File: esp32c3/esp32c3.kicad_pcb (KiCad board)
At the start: 2 copper layers, 20.9 x 32.9 mm, 29 parts, among them J1 A1501WR-S-2P, J2 Conn_01x06, J3 Conn_01x05, SW1 wake up, U1 ESP32-C3-WROOM-02, U2 AHT10, U3 LIS2DH, U4 HX6306

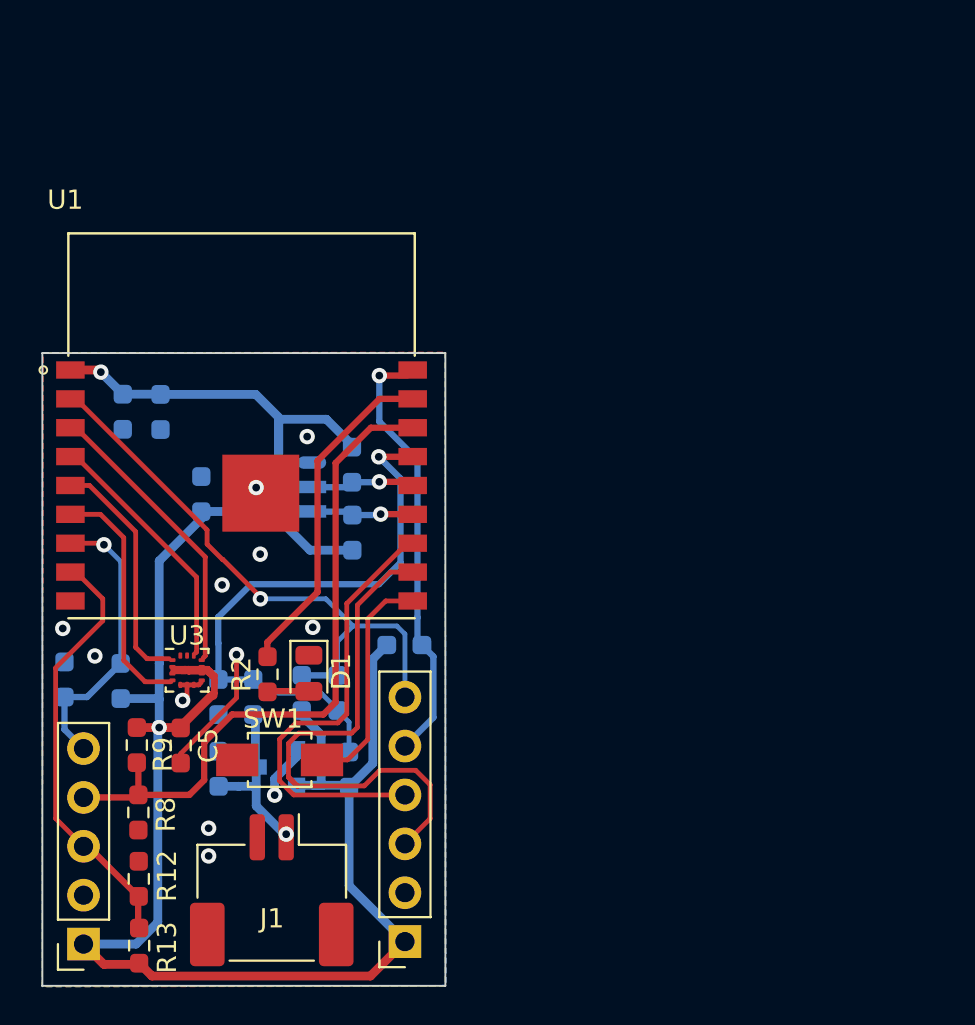
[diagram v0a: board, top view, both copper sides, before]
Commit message: Place components on one side
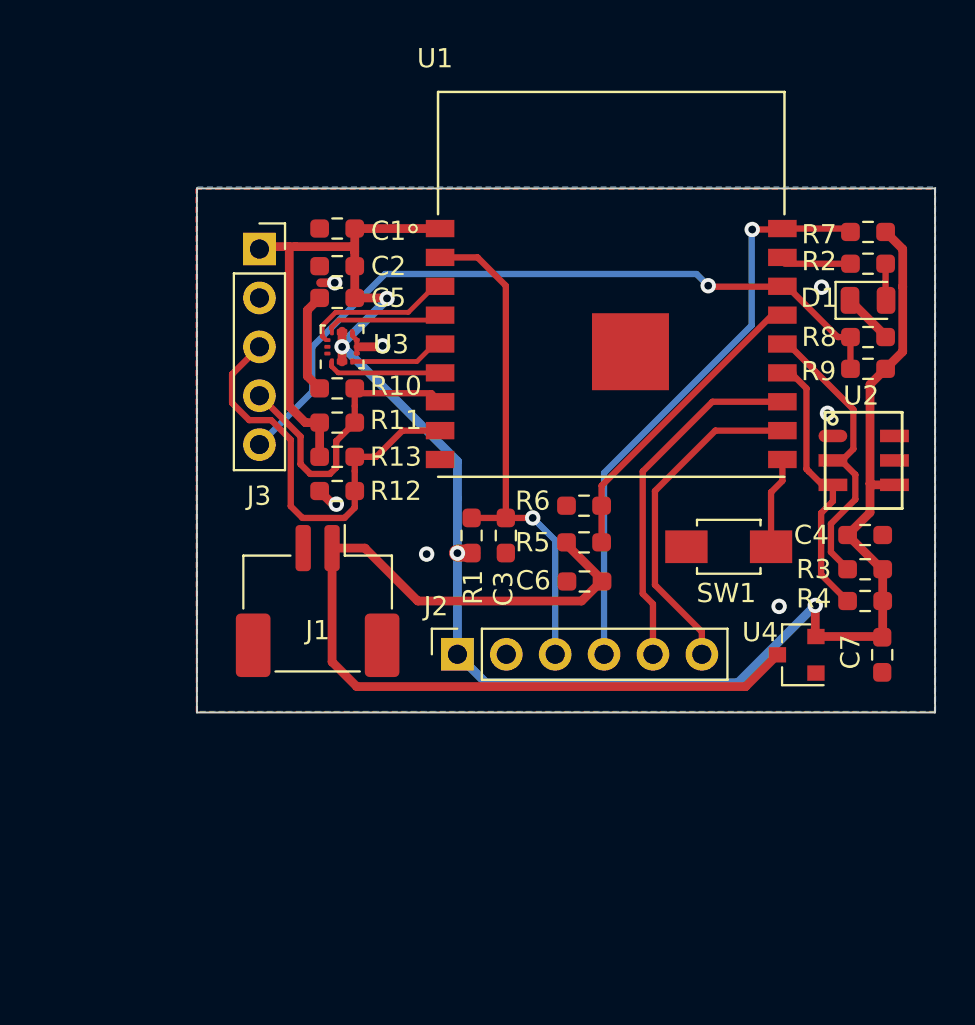
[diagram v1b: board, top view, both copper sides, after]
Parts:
- C1, C2, C3, C4, C6, C7, R1, R10, R11, R3, R4, R5, R6, R7, U2, U4: moved to F.Cu
- moved R8 45.2 mm to (75.8, 76.7), turned to 0 degrees
- moved R9 42.7 mm to (75.8, 78.4), turned to 0 degrees
- moved R2 37.8 mm to (75.8, 72.9), turned to 0 degrees
- moved J3 37.3 mm to (44.2, 72.1), turned to 0 degrees
- moved D1 34.9 mm to (75.8, 74.8), turned to 0 degrees
- moved C4 34.6 mm to (75.7, 87.0), turned to 0 degrees
- moved R7 32.3 mm to (75.8, 71.2), turned to 0 degrees
- moved U2 31.0 mm to (75.9, 83.1), turned to 0 degrees
- moved C7 28.3 mm to (76.6, 93.2), turned to -90 degrees
- moved U4 27.6 mm to (72.1, 93.2)
- moved R13 27.4 mm to (48.3, 82.9), turned to 180 degrees
- moved R3 27.2 mm to (75.7, 88.8), turned to 180 degrees
- moved R4 26.9 mm to (75.7, 90.4), turned to 180 degrees
- moved SW1 25.8 mm to (68.6, 87.6)
- moved C5 24.6 mm to (48.3, 74.7), turned to 180 degrees
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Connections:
- J2 pad 3: RXD -> EN
- J2 pad 4: TXD -> IO0
- J2 pad 5: IO0 -> TXD
- J2 pad 6: EN -> RXD
- J3 pad 4: IO2 -> IO8
- J3 pad 5: IO8 -> IO2
- U1 pad 3: INT2 -> INT1
- U1 pad 4: INT1 -> INT2
- U1 pad 5: SCL -> SDA
- U1 pad 6: SDA -> SCL
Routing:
- net V_In: track 8.96 -> 48.7 mm, vias 1 -> 0
- net LED: track 17.7 -> 3.88 mm
- net 3.3V: track 116.4 -> 102.8 mm, vias 2 -> 4
- net RXD: track 28.8 -> 17.4 mm
- net SDA_AHT10: track 5.29 -> 15.9 mm, vias 1 -> 0
- net SCL_AHT10: track 5.19 -> 14.4 mm, vias 1 -> 0
- net INT2: track 15.1 -> 5.98 mm
- net INT: track 12.7 -> 4.78 mm
- net IO0: track 23.2 -> 31.0 mm
- net SDA: track 12.6 -> 4.92 mm
- net ADC: track 23.4 -> 16.0 mm, vias 1 -> 0
- net SCL: track 12.4 -> 6.03 mm
- net GND: track 17.7 -> 12.3 mm, vias 12 -> 7
- net INT1: track 13.1 -> 7.74 mm
- net TXD: track 23.5 -> 18.5 mm
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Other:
- board size 20.9 x 32.9 mm -> 38.4 x 27.2 mm

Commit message: Complete LIS2DH12 modification
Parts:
- added C8: 0.1uF, Resistor_SMD:R_0603_1608Metric_Pad0.98x0.95mm_HandSolder, F.Cu at (47.9, 75.0)
- added C9: 0.1uF, Resistor_SMD:R_0603_1608Metric_Pad0.98x0.95mm_HandSolder, F.Cu at (47.9, 77.6)
- C5: value 100nF -> 10uF
- U3: footprint Package_LGA:LGA-14_2x2mm_P0.35mm_LayoutBorder3x4y -> Package_LGA:LGA-12_2x2mm_P0.5mm
- moved C2 2.80 mm to (50.9, 72.0), turned to 90 degrees
- moved U3 2.62 mm to (51.1, 77.2)
- moved C5 1.69 mm to (47.9, 73.0)
- moved C1 0.38 mm to (47.9, 71.1)
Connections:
- U3 pad 3: 3.3V -> GND
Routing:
- net GND: track 12.3 -> 3.82 mm, vias 7 -> 5
- net 3.3V: track 102.8 -> 97.7 mm
- net SDA: track 4.92 -> 2.55 mm
- net SCL: track 6.03 -> 3.81 mm
- net INT2: track 5.98 -> 5.17 mm
- net INT1: track 7.74 -> 7.05 mm
- removed copper zone on B.Cu, net GND
- removed copper zone on F.Cu, net GND

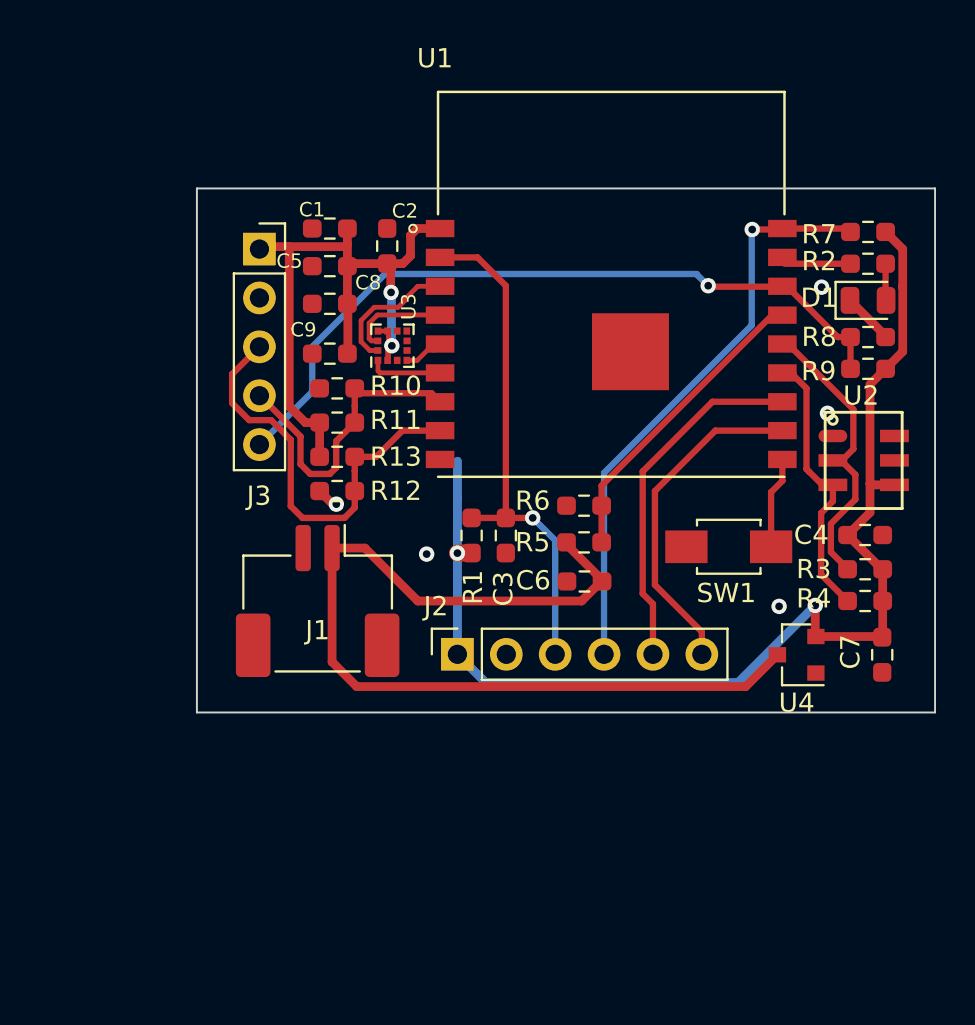
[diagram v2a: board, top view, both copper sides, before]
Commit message: Complete LIS2DH12 modification
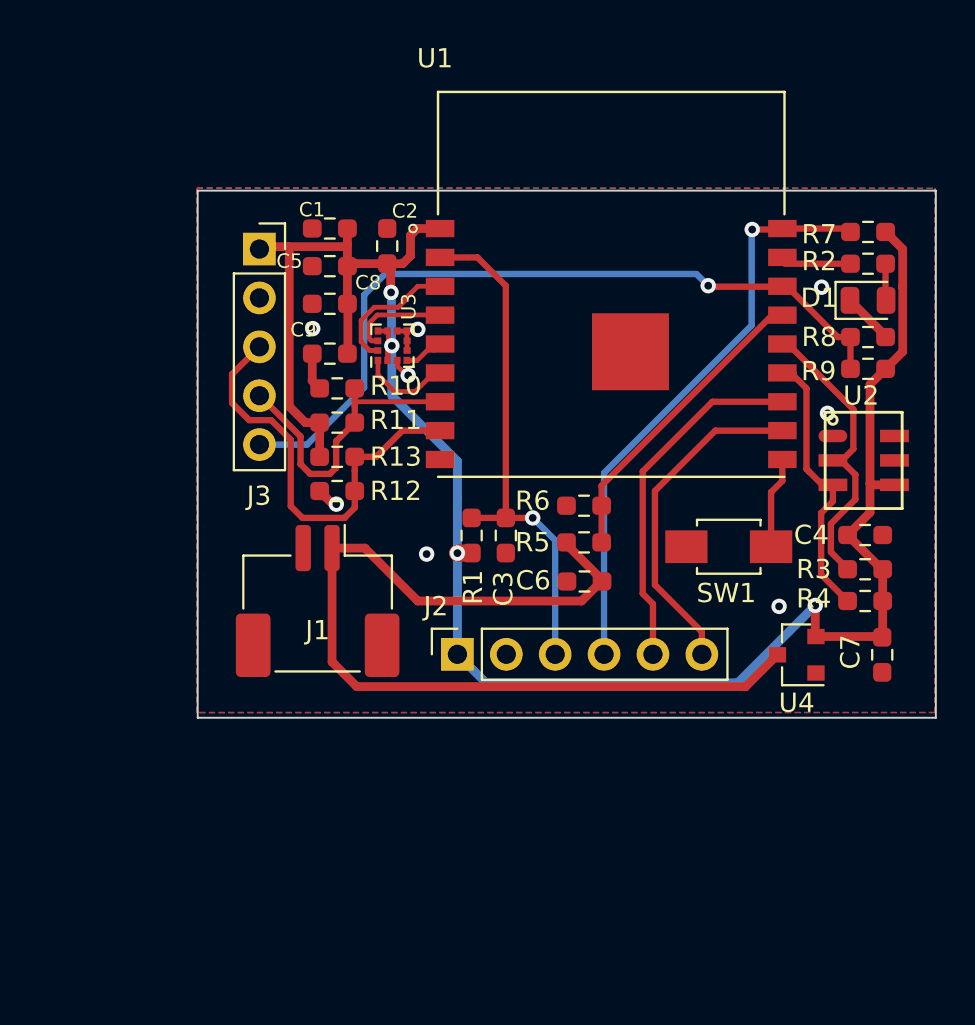
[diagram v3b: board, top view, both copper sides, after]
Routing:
- net 3.3V: track 97.7 -> 105.1 mm
- net GND: track 3.82 -> 8.98 mm, vias 5 -> 8
- net IO2: track 38.8 -> 40.2 mm
- net SCL: track 3.81 -> 5.19 mm
- added copper zone on B.Cu, net GND
- added copper zone on F.Cu, net GND
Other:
- board size 38.4 x 27.2 mm -> 38.4 x 27.4 mm
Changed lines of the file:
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@@
     )
   )
-  (gr_rect (start 40.9702 68.9864) (end 79.3242 96.2152) (layer "Edge.Cuts") (width 0.1) (fill none))
+  (gr_rect (start 41.013 69.1012) (end 79.367 96.49) (layer "Edge.Cuts") (width 0.1) (fill none))
   (segment (start 76.604495 88.773) (end 76.604495 90.424) (width 0.4572) (layer "F.Cu") (net 1))
   (segment (start 74.779505 86.82449) (end 74.77951 86.82449) (width 0.4572) (layer "F.Cu") (net 1))
@@
   (segment (start 54.507994 83.160006) (end 54.507994 85.090406) (width 0.4572) (layer "B.Cu") (net 1))
   (segment (start 51.06 74.39) (end 51.08 74.41) (width 0.4572) (layer "B.Cu") (net 1))
+  (segment (start 51.100126 77.161161) (end 51.100126 79.752139) (width 0.4572) (layer "B.Cu") (net 1))
   (segment (start 51.08 74.41) (end 51.08 77.141024) (width 0.4572) (layer "B.Cu") (net 1))
   (segment (start 54.507994 87.935206) (end 54.507994 93.193006) (width 0.4572) (layer "B.Cu") (net 1))
   (segment (start 69.088 94.6658) (end 55.9808 94.6658) (width 0.4572) (layer "B.Cu") (net 1))
+  (segment (start 51.100126 79.752139) (end 54.507994 83.160006) (width 0.4572) (layer "B.Cu") (net 1))
   (segment (start 48.029673 85.391193) (end 47.347505 84.709) (width 0.4572) (layer "F.Cu") (net 2))
+  (segment (start 52.365504 76.394496) (end 52.45 76.31) (width 0.25) (layer "F.Cu") (net 2))
   (segment (start 76.75499 76.653009) (end 74.904981 74.803) (width 0.4572) (layer "F.Cu") (net 2))
+  (segment (start 51.879997 76.394496) (end 52.365504 76.394496) (width 0.25) (layer "F.Cu") (net 2))
+  (segment (start 51.379997 76.394496) (end 51.879997 76.394496) (width 0.25) (layer "F.Cu") (net 2))
+  (segment (start 47.347505 79.375) (end 46.949995 78.97749) (width 0.4572) (layer "F.Cu") (net 2))
+  (segment (start 51.95 78.7) (end 51.87 78.7) (width 0.25) (layer "F.Cu") (net 2))
+  (segment (start 51.879997 76.894496) (end 51.892497 76.906996) (width 0.25) (layer "F.Cu") (net 2))
   (segment (start 48.215383 85.391184) (end 48.029684 85.391184) (width 0.25) (layer "F.Cu") (net 2))
   (segment (start 76.754995 76.708) (end 76.754995 76.653005) (width 0.25) (layer "F.Cu") (net 2))
+  (segment (start 46.95 78.9775) (end 46.9665 78.961) (width 0.25) (layer "F.Cu") (net 2))
+  (segment (start 46.966505 78.961005) (end 46.966505 77.5716) (width 0.4572) (layer "F.Cu") (net 2))
+  (segment (start 51.87 78.7) (end 51.379997 78.209997) (width 0.25) (layer "F.Cu") (net 2))
+  (segment (start 51.892497 76.906996) (end 51.892497 77.406996) (width 0.25) (layer "F.Cu") (net 2))
+  (segment (start 51.879997 76.394496) (end 51.879997 76.894496) (width 0.25) (layer "F.Cu") (net 2))
+  (segment (start 51.379997 78.209997) (end 51.379997 77.919496) (width 0.25) (layer "F.Cu") (net 2))
+  (via (at 51.95 78.7) (size 0.8) (drill 0.4) (layers "F.Cu" "B.Cu") (free) (net 2))
+  (via (at 52.45 76.31) (size 0.8) (drill 0.4) (layers "F.Cu" "B.Cu") (free) (net 2))
   (via (at 52.9082 87.9856) (size 0.8) (drill 0.4) (layers "F.Cu" "B.Cu") (free) (net 2))
   (via (at 71.2216 90.7034) (size 0.8) (drill 0.4) (layers "F.Cu" "B.Cu") (free) (net 2))
@@
   (via (at 73.4314 74.1172) (size 0.8) (drill 0.4) (layers "F.Cu" "B.Cu") (free) (net 2))
   (via (at 48.215383 85.391184) (size 0.8) (drill 0.4) (layers "F.Cu" "B.Cu") (free) (net 2))
+  (via (at 46.99 76.27) (size 0.8) (drill 0.4) (layers "F.Cu" "B.Cu") (free) (net 2))
   (segment (start 53.607487 72.57001) (end 55.55201 72.57001) (width 0.3302) (layer "F.Cu") (net 3))
   (segment (start 55.245 86.106) (end 57.023 86.106) (width 0.3302) (layer "F.Cu") (net 3))
@@
   (segment (start 71.631607 74.070007) (end 74.2696 76.708) (width 0.3302) (layer "F.Cu") (net 8))
   (via (at 67.5386 74.041) (size 0.8) (drill 0.4) (layers "F.Cu" "B.Cu") (net 8))
-  (segment (start 50.7492 73.4314) (end 46.9646 77.216) (width 0.3302) (layer "B.Cu") (net 8))
-  (segment (start 46.9646 77.216) (end 46.9646 79.552394) (width 0.3302) (layer "B.Cu") (net 8))
+  (segment (start 46.694 82.296) (end 44.220994 82.296) (width 0.3302) (layer "B.Cu") (net 8))
+  (segment (start 50.7492 73.4314) (end 49.66 74.5206) (width 0.3302) (layer "B.Cu") (net 8))
+  (segment (start 49.66 79.33) (end 46.694 82.296) (width 0.3302) (layer "B.Cu") (net 8))
+  (segment (start 66.929 73.4314) (end 50.7492 73.4314) (width 0.3302) (layer "B.Cu") (net 8))
   (segment (start 67.5386 74.041) (end 66.929 73.4314) (width 0.3302) (layer "B.Cu") (net 8))
-  (segment (start 46.9646 79.552394) (end 44.220994 82.296) (width 0.3302) (layer "B.Cu") (net 8))
-  (segment (start 66.929 73.4314) (end 50.7492 73.4314) (width 0.3302) (layer "B.Cu") (net 8))
+  (segment (start 49.66 74.5206) (end 49.66 79.33) (width 0.3302) (layer "B.Cu") (net 8))
   (segment (start 48.2092 83.4898) (end 48.2092 82.1163) (width 0.3302) (layer "F.Cu") (net 9))
   (segment (start 46.355 81.871268) (end 46.355 83.312) (width 0.3302) (layer "F.Cu") (net 9))
+  (segment (start 53.6075 80.07) (end 49.22 80.07) (width 0.25) (layer "F.Cu") (net 9))
   (segment (start 44.221 79.756) (end 44.239732 79.756) (width 0.3302) (layer "F.Cu") (net 9))
+  (segment (start 49.172495 79.375) (end 49.172495 80.022495) (width 0.3302) (layer "F.Cu") (net 9))
+  (segment (start 49.172495 80.022495) (end 49.172495 80.287495) (width 0.3302) (layer "F.Cu") (net 9))
   (segment (start 46.863 83.82) (end 47.879 83.82) (width 0.3302) (layer "F.Cu") (net 9))
   (segment (start 46.355 83.312) (end 46.863 83.82) (width 0.3302) (layer "F.Cu") (net 9))
   (segment (start 44.239732 79.756) (end 46.355 81.871268) (width 0.3302) (layer "F.Cu") (net 9))
   (segment (start 47.879 83.82) (end 48.2092 83.4898) (width 0.3302) (layer "F.Cu") (net 9))
-  (segment (start 49.172495 79.375) (end 49.172495 80.287495) (width 0.3302) (layer "F.Cu") (net 9))
-  (segment (start 49.4265 79.629) (end 53.166493 79.629) (width 0.3302) (layer "F.Cu") (net 9))
-  (segment (start 53.166493 79.629) (end 53.293493 79.756) (width 0.3302) (layer "F.Cu") (net 9))
   (segment (start 48.2092 82.1163) (end 49.1725 81.153) (width 0.3302) (layer "F.Cu") (net 9))
+  (segment (start 49.22 80.07) (end 49.172495 80.022495) (width 0.25) (layer "F.Cu") (net 9))
   (segment (start 49.172495 80.287495) (end 49.172495 81.153) (width 0.3302) (layer "F.Cu") (net 9))
-  (segment (start 49.1725 79.375) (end 49.4265 79.629) (width 0.3302) (layer "F.Cu") (net 9))
   (segment (start 53.2935 79.756) (end 53.6075 80.07) (width 0.25) (layer "F.Cu") (net 9))
   (segment (start 42.799 78.637994) (end 42.799 80.137) (width 0.3302) (layer "F.Cu") (net 10))
@@
   (segment (start 53.2775 77.4) (end 53.6075 77.07) (width 0.25) (layer "F.Cu") (net 16))
   (segment (start 53.268992 77.07) (end 52.419496 77.919496) (width 0.25) (layer "F.Cu") (net 16))
-  (segment (start 53.6075 78.57) (end 50.49 78.57) (width 0.25) (layer "F.Cu") (net 17))
-  (segment (start 50.379997 78.459997) (end 50.379997 77.919496) (width 0.25) (layer "F.Cu") (net 17))
-  (segment (start 50.49 78.57) (end 50.379997 78.459997) (width 0.25) (layer "F.Cu") (net 17))
+  (segment (start 53.28 78.57) (end 53.6075 78.57) (width 0.25) (layer "F.Cu") (net 17))
+  (segment (start 52.31 79.54) (end 53.28 78.57) (width 0.25) (layer "F.Cu") (net 17))
+  (segment (start 51.25 79.54) (end 52.31 79.54) (width 0.25) (layer "F.Cu") (net 17))
+  (segment (start 50.379997 77.919496) (end 50.379997 78.669997) (width 0.25) (layer "F.Cu") (net 17))
+  (segment (start 50.379997 78.669997) (end 51.25 79.54) (width 0.25) (layer "F.Cu") (net 17))
+  (segment (start 53.6075 78.57) (end 53.2875 78.89) (width 0.25) (layer "F.Cu") (net 17))
   (segment (start 49.5 75.844688) (end 49.5 76.95) (width 0.25) (layer "F.Cu") (net 18))
   (segment (start 50.184424 75.160264) (end 49.5 75.844688) (width 0.25) (layer "F.Cu") (net 18))
@@
   (segment (start 62.02299 89.32799) (end 62.02299 89.408) (width 0.4572) (layer "F.Cu") (net 21))
   (segment (start 52.451 90.424) (end 49.700993 87.673993) (width 0.4572) (layer "F.Cu") (net 21))
+  (zone (net 2) (net_name "GND") (layer "F.Cu") (hatch edge 0.508)
+    (connect_pads (clearance 0.508))
+    (min_thickness 0.254) (filled_areas_thickness no)
+    (fill yes (thermal_gap 0.508) (thermal_bridge_width 0.508))
+    (polygon
+      (pts
+        (xy 79.32 68.98)
+        (xy 79.31 96.21)
+        (xy 40.97 96.21)
+        (xy 40.97 68.96)
+      )
+    )
+  )
+  (zone (net 2) (net_name "GND") (layer "B.Cu") (hatch edge 0.508)
+    (connect_pads (clearance 0.508))
+    (min_thickness 0.254) (filled_areas_thickness no)
+    (fill yes (thermal_gap 0.508) (thermal_bridge_width 0.508))
+    (polygon
+      (pts
+        (xy 79.32 68.98)
+        (xy 79.33 96.22)
+        (xy 40.98 96.23)
+        (xy 40.98 68.97)
+      )
+    )
+  )
 )

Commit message: prepare v2.0-alpha-1 for fabrication
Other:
- board text added: "MindDot REV 2.0-alpha-1 [2022-04-22]"
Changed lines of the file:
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@@
-(kicad_pcb (version 20210623) (generator pcbnew)
+(kicad_pcb (version 20211014) (generator pcbnew)
   (general
     (thickness 1.6)
@@
       (outputformat 1)
       (mirror false)
-      (drillshape 1)
+      (drillshape 0)
       (scaleselection 1)
-      (outputdirectory "")
+      (outputdirectory "fabrication/v2.0-alpha-1/")
     )
   )
@@
     (pad "2" smd roundrect locked (at 0.75 2.75 180) (size 0.8 2.4) (layers "F.Cu" "F.Paste" "F.Mask") (roundrect_rratio 0.25)
       (net 2 "GND") (pinfunction "2") (pintype "bidirectional"))
-    (pad "MP" smd roundrect locked (at -3.35 -2.3 180) (size 1.8 3.3) (layers "F.Cu" "F.Paste" "F.Mask") (roundrect_rratio 0.138889))
-    (pad "MP" smd roundrect locked (at 3.35 -2.3 180) (size 1.8 3.3) (layers "F.Cu" "F.Paste" "F.Mask") (roundrect_rratio 0.138889))
+    (pad "MP" smd roundrect locked (at -3.35 -2.3 180) (size 1.8 3.3) (layers "F.Cu" "F.Paste" "F.Mask") (roundrect_rratio 0.1388888889))
+    (pad "MP" smd roundrect locked (at 3.35 -2.3 180) (size 1.8 3.3) (layers "F.Cu" "F.Paste" "F.Mask") (roundrect_rratio 0.1388888889))
     (model "${KISYS3DMOD}/Connector_JST.3dshapes/JST_ZE_BM02B-ZESS-TBT_1x02-1MP_P1.50mm_Vertical.wrl"
       (offset (xyz 0 0 0))
@@
   )
   (gr_rect (start 41.013 69.1012) (end 79.367 96.49) (layer "Edge.Cuts") (width 0.1) (fill none))
+  (gr_text "MindDot REV 2.0-alpha-1 [2022-04-22]" (at 60.9 89.7) (layer "B.SilkS")
+    (effects (font (size 1 1) (thickness 0.15)) (justify mirror))
+  )
   (segment (start 76.604495 88.773) (end 76.604495 90.424) (width 0.4572) (layer "F.Cu") (net 1))
   (segment (start 74.779505 86.82449) (end 74.77951 86.82449) (width 0.4572) (layer "F.Cu") (net 1))
